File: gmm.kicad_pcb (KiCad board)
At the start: 6 copper layers, 70 x 50 mm, 213 parts, among them P1 10144518-061802LF, P2 10144518-061802LF, P3 10144518-061802LF, P4 10144518-061802LF, P5 10144518-061802LF, U1 CCGM1A1, U10 PCA9539AHF, U11 TPS3840DL28DBV, U2 5P49V6965, U3 LM26480SQ, U4 STG3692, U5 STG3692, U6 74LVC1G08, U7 74LVC1G07, U8 STG3692, U9 IS25LQ032B-JNLE, Y1 NX3225SA

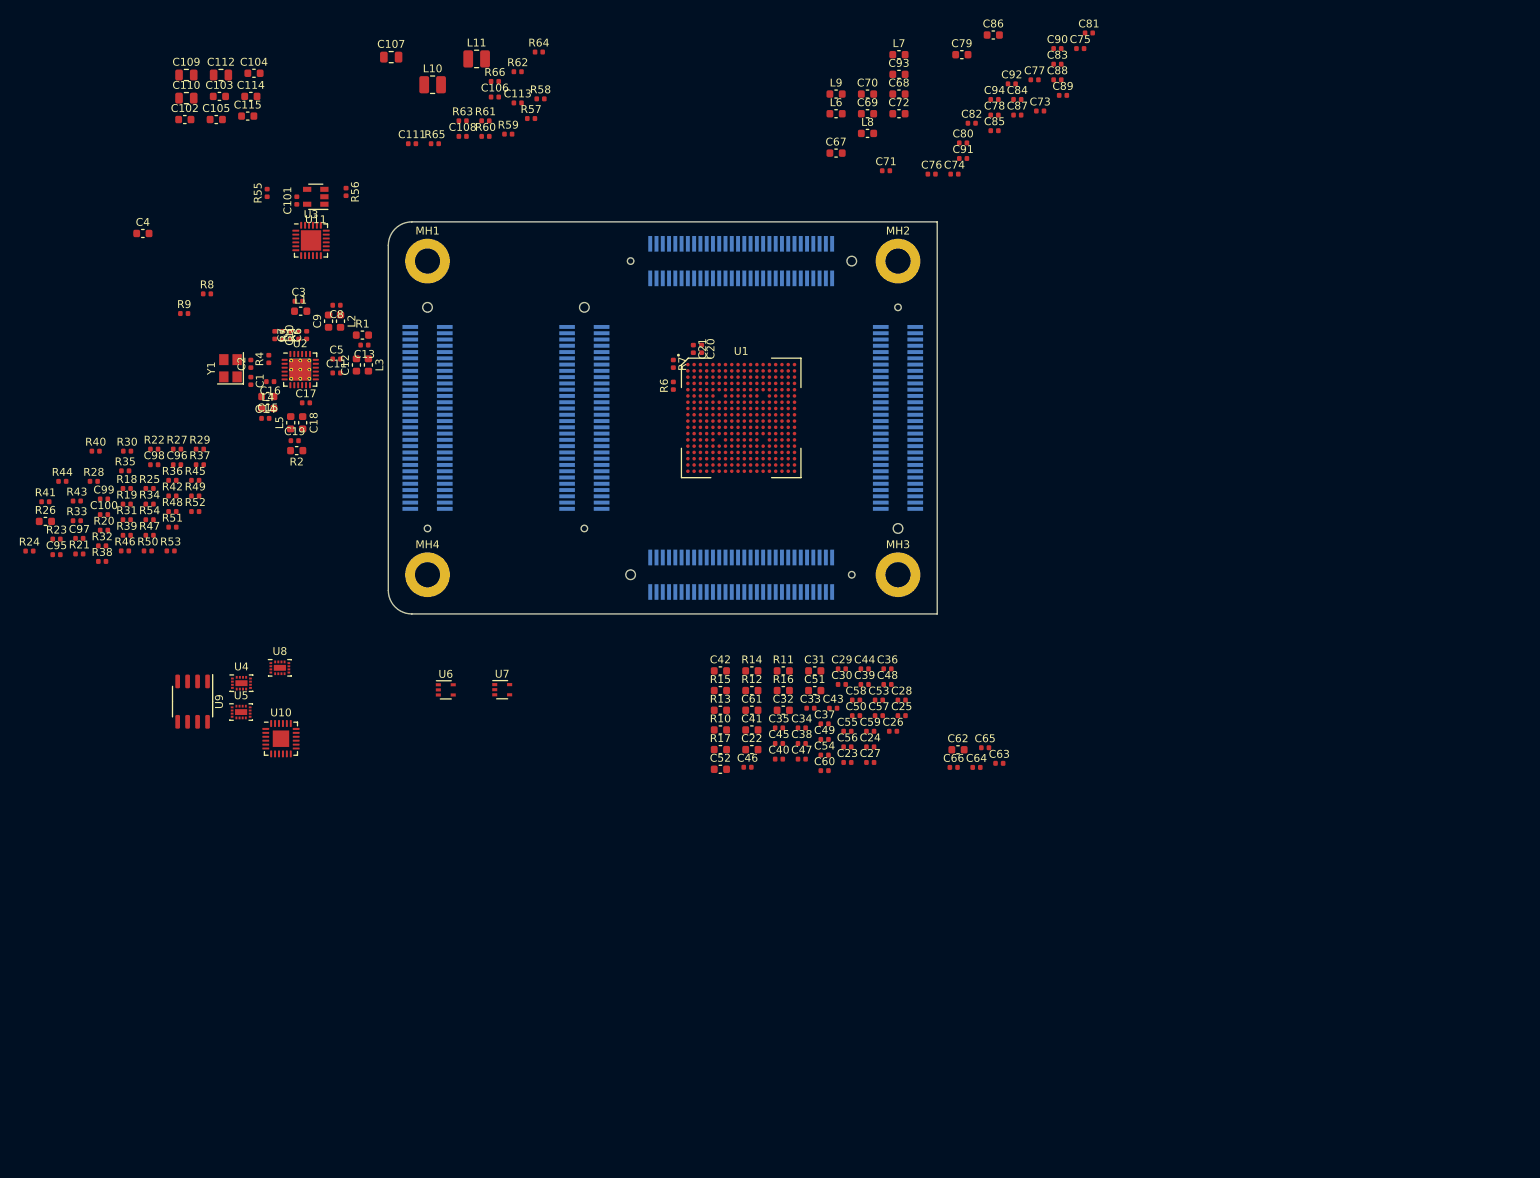
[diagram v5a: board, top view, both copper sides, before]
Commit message: Placement and a bit of FPGA fanout
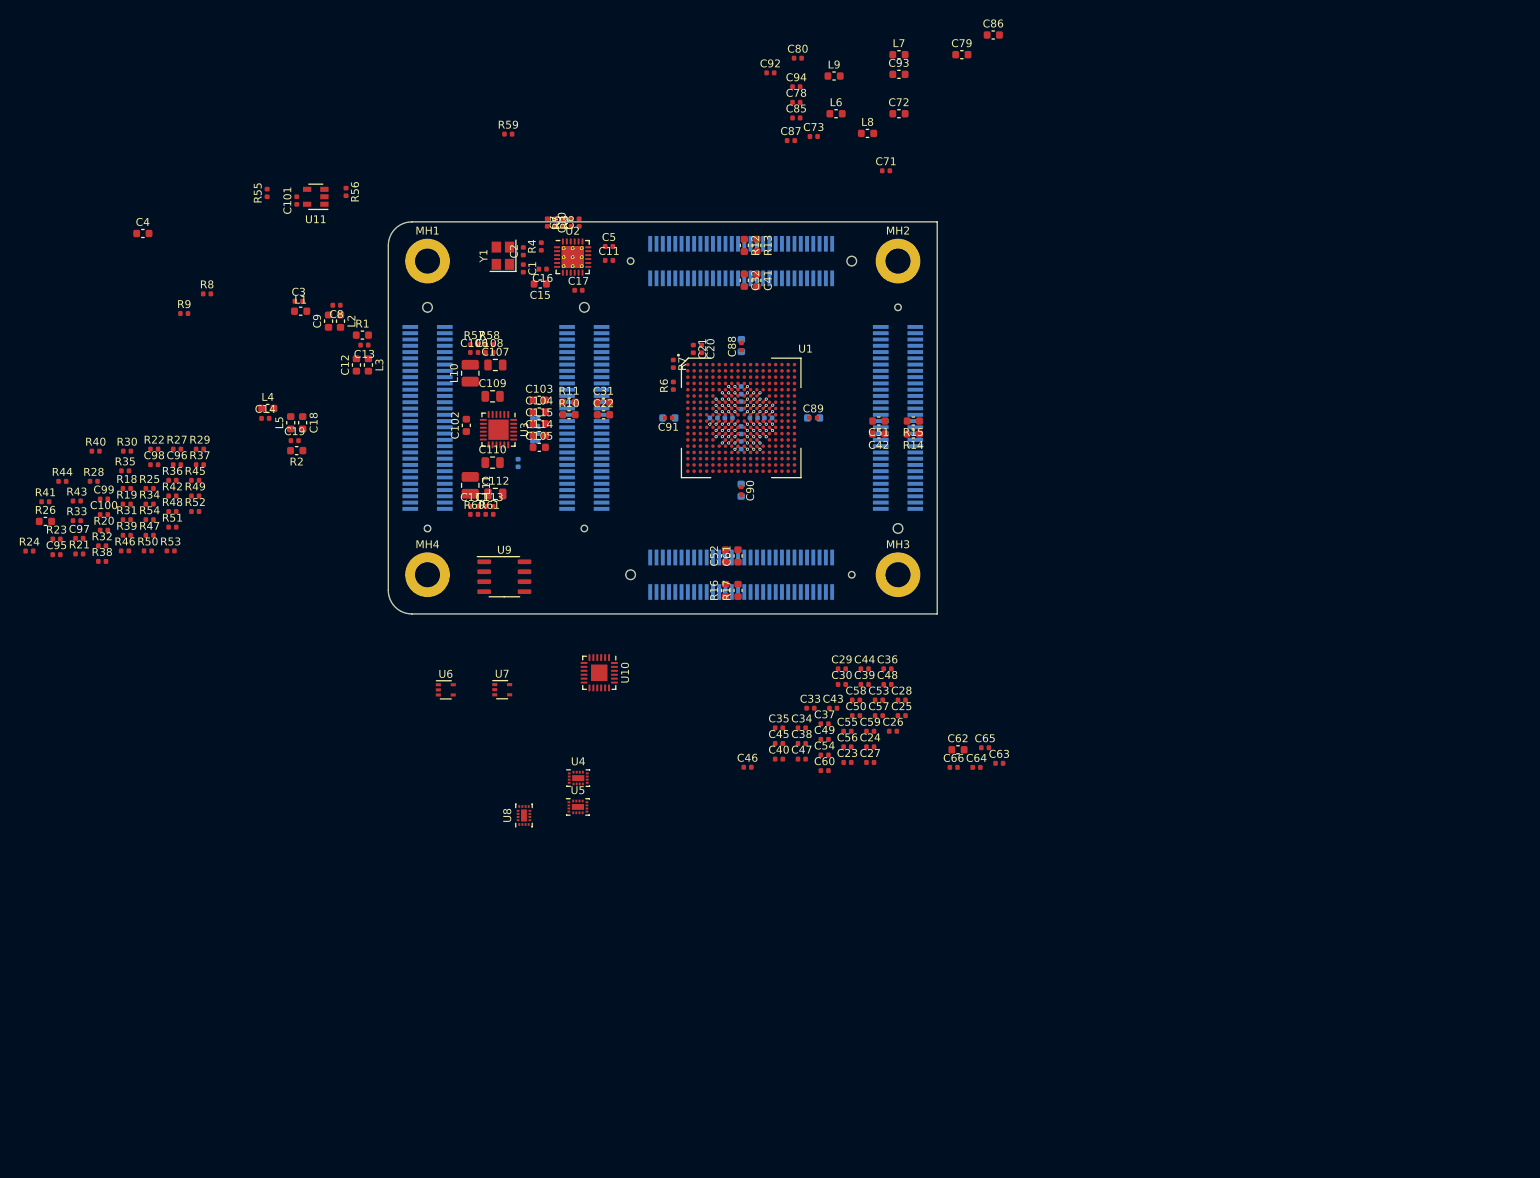
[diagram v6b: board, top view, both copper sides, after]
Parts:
- C67, C68, C69, C70, C74, C75, C76, C77, C81, C82, C83, C84, R62, R63, R64, R65, R66: moved to B.Cu
- moved C90 69.3 mm to (135.0, 114.3), turned to 270 degrees
- moved C81 67.3 mm to (135.0, 106.6), turned to 270 degrees
- moved C112 63.9 mm to (103.7, 114.7)
- moved C75 62.8 mm to (135.0, 103.4), turned to 90 degrees
- moved C83 61.6 mm to (133.4, 105.0), turned to 180 degrees
- moved C110 60.7 mm to (103.3, 110.7)
- moved R13 59.5 mm to (137.0, 83.0), turned to 270 degrees
- moved C105 58.7 mm to (109.2, 108.8)
- moved C41 57.3 mm to (137.0, 87.5), turned to 270 degrees
- moved R12 56.8 mm to (135.4, 83.0), turned to 270 degrees
- moved C114 56.8 mm to (109.2, 107.2)
- moved C109 56.6 mm to (103.3, 102.2)
- moved C104 56.5 mm to (109.2, 104.2)
- moved C103 56.3 mm to (109.2, 102.8)
- moved C84 56.1 mm to (131.5, 105.0), turned to 180 degrees
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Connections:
- P3 pad 27: (no net) -> IO_S2_B1
- P3 pad 29: (no net) -> IO_S2_A1
- U1 pad U15: (no net) -> IO_S2_B1
- U1 pad V15: (no net) -> IO_S2_A1
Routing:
- net GND: track 0.00 -> 21.0 mm, vias 0 -> 37
- net +1V0: track 0.00 -> 12.4 mm, vias 0 -> 22
- net VIO_S1: track 0.00 -> 1.70 mm, vias 0 -> 3
- net VIO_N1: track 0.00 -> 1.13 mm, vias 0 -> 2
- net VIO_E1: track 0.00 -> 1.13 mm, vias 0 -> 2
- net VIO_N2: track 0.00 -> 0.57 mm, vias 0 -> 1
- net +2V5: track 0.00 -> 0.57 mm, vias 0 -> 1
- net VIO_W1: track 0.00 -> 0.57 mm, vias 0 -> 1
- net VIO_S2: track 0.00 -> 0.57 mm, vias 0 -> 1
- net VIO_E2: track 0.00 -> 0.57 mm, vias 0 -> 1
- net VIO_W2: track 0.00 -> 0.57 mm, vias 0 -> 1
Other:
- net class Default: clearance 0.2 -> 0.1; trace_width 0.25 -> 0.15; via_dia 0.8 -> 0.4; via_drill 0.4 -> 0.2
- net class PWR added: clearance 0.1, trace_width 0.2, via_dia 0.4, via_drill 0.2
- rule pad_to_mask_clearance: 0.051 -> 0
- rule trace_clearance: 0.2 -> 0.1
- rule trace_min: 0.2 -> 0.1
- rule via_min_drill: 0.3 -> 0.2

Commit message: Placement -- WIP
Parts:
- C106, C108, C111, C113, R37, R39, R57, R58, R60, R61, U11: moved to B.Cu
- moved C40 70.6 mm to (136.7, 78.0)
- moved C38 69.8 mm to (136.7, 77.0)
- moved C37 69.7 mm to (136.8, 74.9)
- moved C35 68.8 mm to (133.8, 76.0)
- moved C34 68.1 mm to (133.8, 77.0)
- moved C36 65.1 mm to (133.8, 75.0)
- moved C33 64.8 mm to (133.8, 78.0)
- moved C39 64.5 mm to (136.7, 76.0)
- moved R24 63.5 mm to (106.7, 133.4), turned to 90 degrees
- moved R38 56.2 mm to (109.8, 124.1), turned to 270 degrees
- moved R46 54.0 mm to (106.6, 142.0), turned to 270 degrees
- moved C99 53.5 mm to (106.9, 121.9), turned to 180 degrees
- moved R35 52.9 mm to (107.0, 96.3), turned to 90 degrees
- moved C46 52.5 mm to (165.0, 105.9)
- moved R45 51.2 mm to (107.6, 142.0), turned to 270 degrees
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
